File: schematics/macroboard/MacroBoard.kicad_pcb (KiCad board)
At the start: 2 copper layers, 94 x 120.6 mm, 83 parts, among them J1 USB4800-03-A_REVA, J2 Conn_01x08_Male, SW1 SW_Push, SW10 SW_Push, SW11 SW_Push, SW12 SW_Push, SW13 SW_Push, SW14 SW_Push, SW15 SW_Push, SW16 SW_Push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

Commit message: minor cleanup on schematic, hided value labels on switches on keyboard matrix for better readability
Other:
- board text added: "Macroboard v1.1"
- board text removed: "Macroboard v1.0"
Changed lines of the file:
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@@
   )
   (gr_rect (start 16.51 40.64) (end 110.49 161.29) (layer "Edge.Cuts") (width 0.1) (fill none))
-  (gr_text "Macroboard v1.0" (at 90.424 155.448) (layer "F.SilkS")
+  (gr_text "Macroboard v1.1" (at 90.424 155.448) (layer "F.SilkS")
     (effects (font (size 1.5 1.5) (thickness 0.3)))
   )

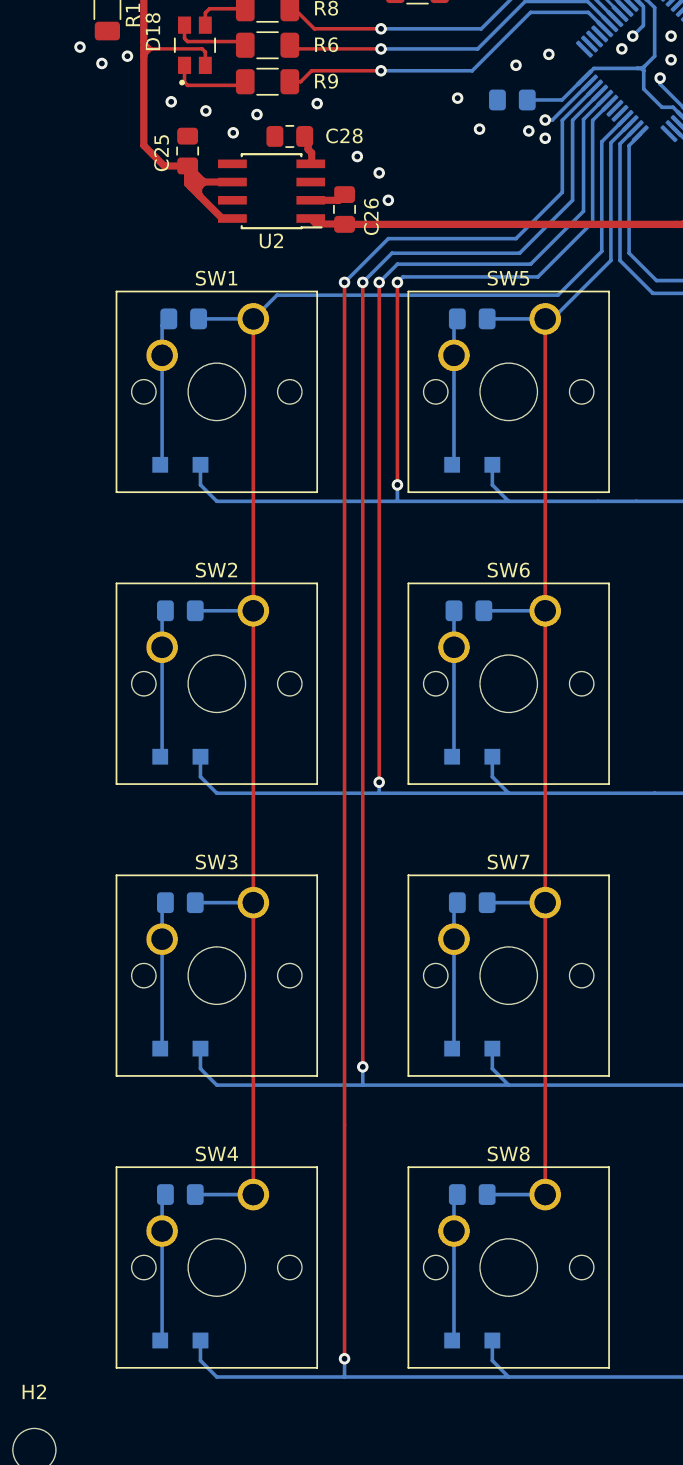
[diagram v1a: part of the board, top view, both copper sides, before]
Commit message: schematic: moved row connections to the side of the pcb
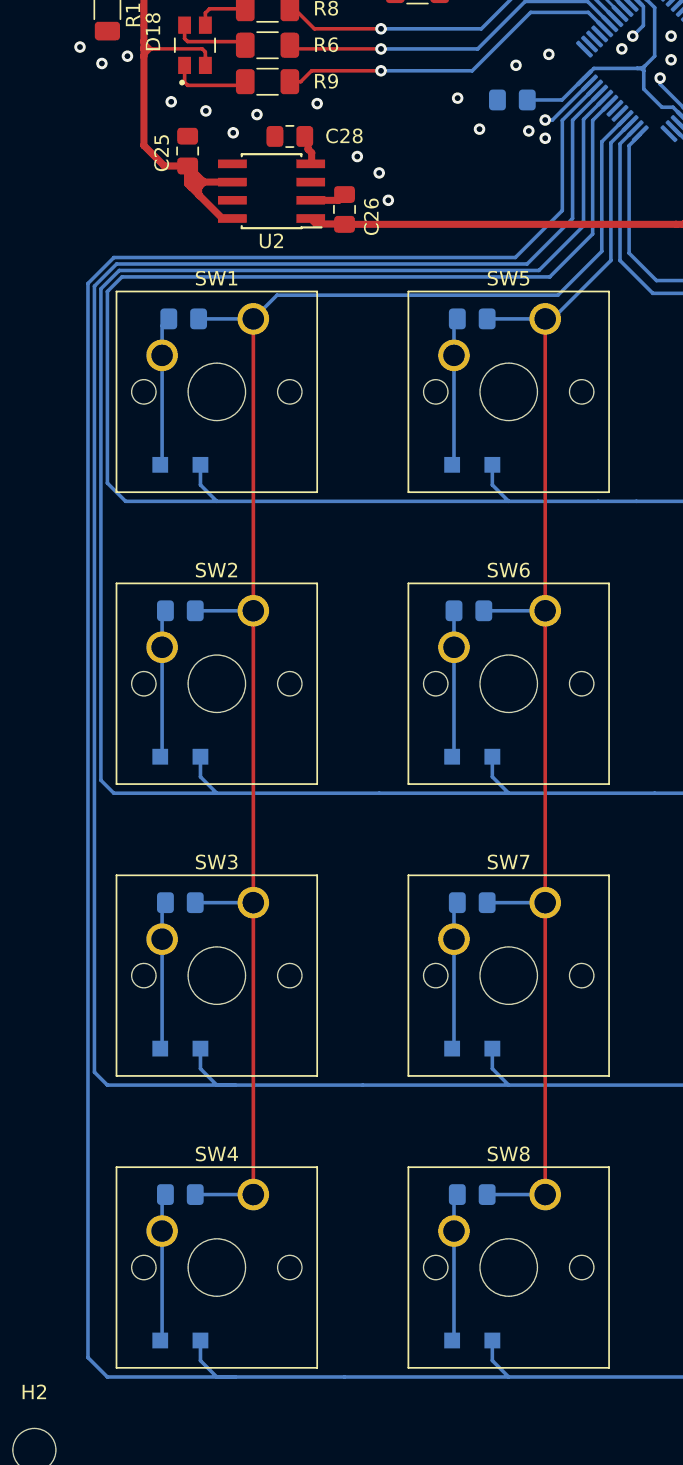
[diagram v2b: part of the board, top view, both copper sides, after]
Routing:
- net ROW2: track 151.8 -> 180.4 mm, vias 2 -> 0
- net ROW3: track 172.9 -> 200.9 mm, vias 2 -> 0
- net ROW1: track 131.0 -> 158.3 mm, vias 2 -> 0
- net ROW0: track 110.1 -> 137.3 mm, vias 2 -> 0
